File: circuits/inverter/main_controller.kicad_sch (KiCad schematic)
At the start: 69 parts

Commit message: converts libraries to Kicad 6 format, updates bridge driver
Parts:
- gave numbers to parts that had none: 8

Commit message: adds interface schematic and NodeMCU symbol for it
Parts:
- added R?: 10k, symbol OSSI_standard_components:Resistor
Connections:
- net +3V3: now also R?.1
- net JTAG_CLK/SWD_CLK/PTA0: now reaches U?.22 (JTAG_CLK/PTA0), X?.4
- net JTAG_TDO/TRACE_SWO/PTA2: now reaches U?.24 (JTAG_TDO/PTA2), X?.6
- net JTAG_TMS/SWD_DIO/PTA3: now reaches U?.25 (JTAG_TMS/PTA3), X?.2
- net JTAG_TMS/SWD_DIO/PTA3: now also R?.2
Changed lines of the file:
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@@
   (junction (at 83.82 124.46) (diameter 0) (color 0 0 0 0)
   )
+  (junction (at 36.83 77.47) (diameter 0) (color 0 0 0 0)
+  )
   (junction (at 115.57 144.78) (diameter 0) (color 0 0 0 0)
   )
@@
   (junction (at 219.71 158.75) (diameter 0) (color 0 0 0 0)
   )
+  (junction (at 16.51 71.12) (diameter 0) (color 0 0 0 0)
+  )
   (junction (at 36.83 102.87) (diameter 0) (color 0 0 0 0)
   )
@@
     (stroke (width 0) (type default) (color 0 0 0 0))
   )
+  (wire (pts (xy 16.51 71.12) (xy 16.51 68.58))
+    (stroke (width 0) (type default) (color 0 0 0 0))
+  )
   (wire (pts (xy 116.84 97.79) (xy 125.73 97.79))
     (stroke (width 0) (type default) (color 0 0 0 0))
@@
     (stroke (width 0) (type default) (color 0 0 0 0))
   )
-  (wire (pts (xy 16.51 77.47) (xy 16.51 73.66))
+  (wire (pts (xy 16.51 77.47) (xy 16.51 71.12))
     (stroke (width 0) (type default) (color 0 0 0 0))
   )
@@
     (stroke (width 0) (type default) (color 0 0 0 0))
   )
+  (wire (pts (xy 16.51 71.12) (xy 24.13 71.12))
+    (stroke (width 0) (type default) (color 0 0 0 0))
+  )
   (wire (pts (xy 102.87 179.07) (xy 102.87 182.88))
     (stroke (width 0) (type default) (color 0 0 0 0))
@@
     (stroke (width 0) (type default) (color 0 0 0 0))
   )
+  (wire (pts (xy 36.83 71.12) (xy 36.83 77.47))
+    (stroke (width 0) (type default) (color 0 0 0 0))
+  )
   (wire (pts (xy 200.66 86.36) (xy 218.44 86.36))
     (stroke (width 0) (type default) (color 0 0 0 0))
@@
     (stroke (width 0) (type default) (color 0 0 0 0))
   )
+  (wire (pts (xy 36.83 77.47) (xy 74.93 77.47))
+    (stroke (width 0) (type default) (color 0 0 0 0))
+  )
   (wire (pts (xy 99.06 35.56) (xy 106.68 35.56))
     (stroke (width 0) (type default) (color 0 0 0 0))
@@
     (stroke (width 0) (type default) (color 0 0 0 0))
   )
+  (wire (pts (xy 34.29 71.12) (xy 36.83 71.12))
+    (stroke (width 0) (type default) (color 0 0 0 0))
+  )
   (wire (pts (xy 219.71 143.51) (xy 231.14 143.51))
     (stroke (width 0) (type default) (color 0 0 0 0))
@@
     (stroke (width 0) (type default) (color 0 0 0 0))
   )
-  (wire (pts (xy 34.29 77.47) (xy 74.93 77.47))
+  (wire (pts (xy 34.29 77.47) (xy 36.83 77.47))
     (stroke (width 0) (type default) (color 0 0 0 0))
   )
@@
     (effects (font (size 1.524 1.524)) (justify left bottom))
   )
-  (text "JTAG programmer connection" (at 22.86 71.12 0)
+  (text "JTAG programmer connection" (at 19.05 66.04 0)
     (effects (font (size 1.524 1.524)) (justify left bottom))
   )
@@
     (effects (font (size 1.27 1.27)) (justify left bottom))
   )
+  (label "JTAG_TDO{slash}TRACE_SWO{slash}PTA2" (at 39.37 82.55 0)
+    (effects (font (size 0.9906 0.9906)) (justify left bottom))
+  )
+  (label "JTAG_CLK{slash}SWD_CLK{slash}PTA0" (at 39.37 80.01 0)
+    (effects (font (size 0.9906 0.9906)) (justify left bottom))
+  )
+  (label "JTAG_TMS{slash}SWD_DIO{slash}PTA3" (at 39.37 77.47 0)
+    (effects (font (size 0.9906 0.9906)) (justify left bottom))
+  )
   (hierarchical_label "Bridge_T2" (shape output) (at 132.08 22.86 0)
     (effects (font (size 1.524 1.524)) (justify left))
@@
     (pin "1")
   )
-  (symbol (lib_id "OSSI_standard_components:+3V3") (at 16.51 73.66 0) (unit 1)
+  (symbol (lib_id "OSSI_standard_components:+3V3") (at 16.51 68.58 0) (unit 1)
     (in_bom yes) (on_board yes)
-    (property "Reference" "#+3V0101" (id 0) (at 16.51 66.675 0)
+    (property "Reference" "#+3V0101" (id 0) (at 16.51 61.595 0)
       (effects (font (size 1.524 1.524)) hide)
     )
-    (property "Value" "+3V3" (id 1) (at 16.51 68.58 0)
+    (property "Value" "+3V3" (id 1) (at 16.51 63.5 0)
       (effects (font (size 1.1938 1.1938) bold))
     )
-    (property "Footprint" "" (id 2) (at 16.51 73.66 0)
+    (property "Footprint" "" (id 2) (at 16.51 68.58 0)
       (effects (font (size 1.524 1.524)))
     )
-    (property "Datasheet" "" (id 3) (at 16.51 73.66 0)
+    (property "Datasheet" "" (id 3) (at 16.51 68.58 0)
       (effects (font (size 1.524 1.524)))
     )
@@
       (effects (font (size 0.889 0.889)) (justify left) hide)
     )
+    (pin "1")
+    (pin "2")
+  )
+  (symbol (lib_id "OSSI_standard_components:Resistor") (at 29.21 71.12 0) (mirror x) (unit 1)
+    (in_bom yes) (on_board yes)
+    (property "Reference" "R?" (id 0) (at 29.21 69.215 0)
+      (effects (font (size 0.9906 0.9906)))
+    )
+    (property "Value" "10k" (id 1) (at 29.21 71.12 0)
+      (effects (font (size 0.9906 0.9906)))
+    )
+    (property "Footprint" "" (id 2) (at 29.21 72.898 0)
+      (effects (font (size 0.889 0.889)))
+    )
+    (property "Datasheet" "" (id 3) (at 29.21 71.12 0)
+      (effects (font (size 1.524 1.524)))
+    )
+    (property "Tolerance" "%" (id 4) (at 29.21 74.295 0)
+      (effects (font (size 0.889 0.889)) hide)
+    )
+    (property "Manufacturer" "M" (id 5) (at 32.385 74.295 0)
+      (effects (font (size 0.889 0.889)) (justify left) hide)
+    )
+    (property "Partnumber" "P" (id 6) (at 32.385 73.025 0)
+      (effects (font (size 0.889 0.889)) (justify left) hide)
+    )
+    (property "Supplier" "S" (id 7) (at 32.385 75.565 0)
+      (effects (font (size 0.889 0.889)) (justify left) hide)
+    )
+    (property "Order No." "O.No." (id 8) (at 32.385 76.835 0)
+      (effects (font (size 0.889 0.889)) (justify left) hide)
+    )

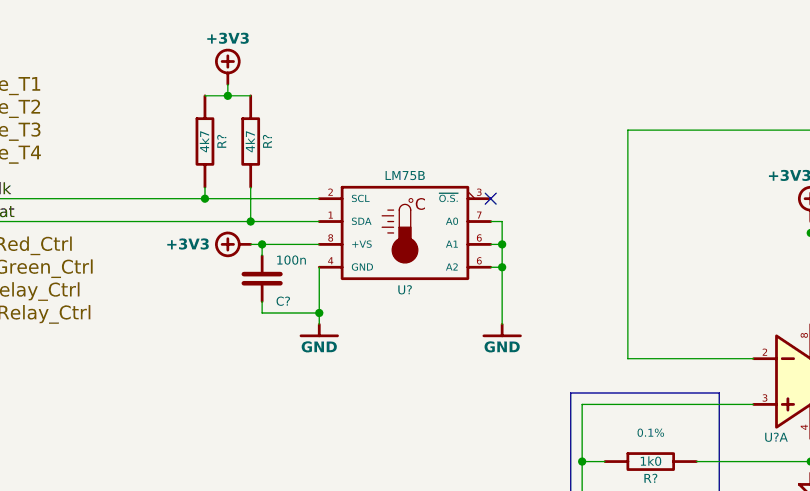
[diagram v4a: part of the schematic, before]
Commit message: converts the project to Kicad 7
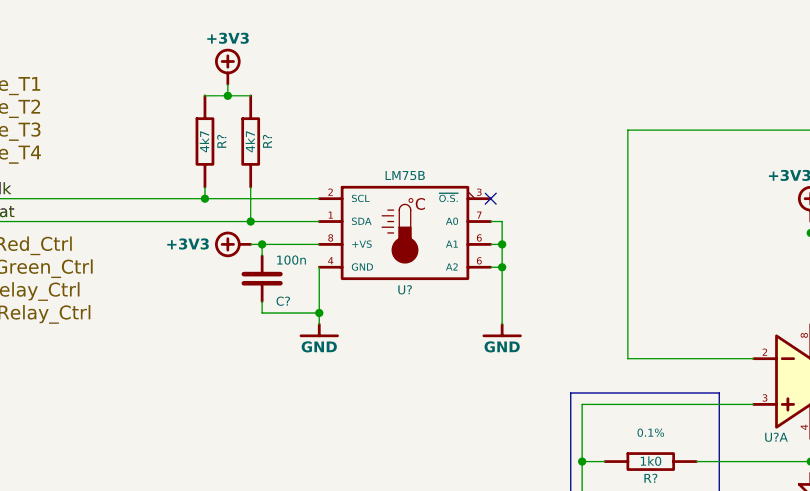
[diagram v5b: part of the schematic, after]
